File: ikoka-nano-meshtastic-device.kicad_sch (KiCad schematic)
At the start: 10 parts, among them J1 JST_2mm_LiPo, J2 JST_2mm_LiPo, J3 Qwiic_RA, U1 Seeed Studio XIAO nRF52840, U2 E22-900M30S

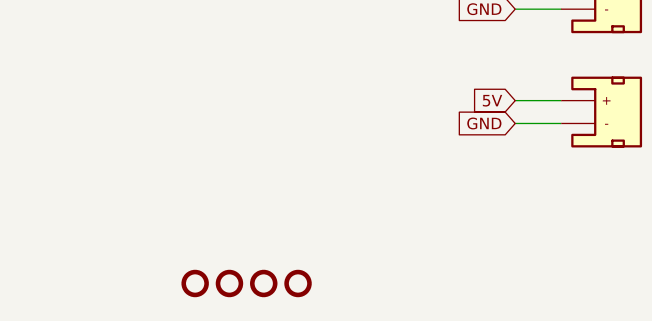
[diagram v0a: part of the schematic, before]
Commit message: Update schematic with LCSC part numbers
Signed-off-by: Andrew Yong <me@ndoo.sg>
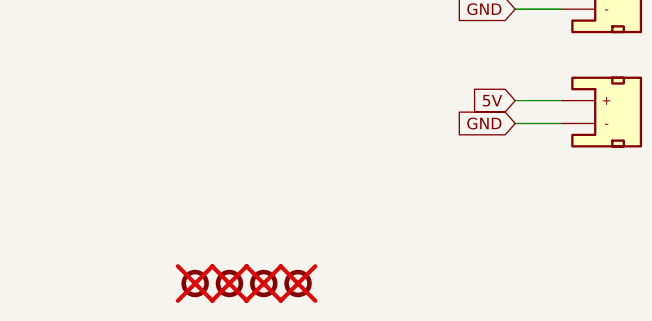
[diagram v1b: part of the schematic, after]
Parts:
- C1: LCSC (none) -> C77085
- J1, J2: LCSC (none) -> C295747
- J3: LCSC (none) -> C160404
- ST1, ST2, ST3, ST4: now not fitted; now left out of the parts list
- U1: LCSC (none) -> C17209540
- U2: LCSC (none) -> C411294
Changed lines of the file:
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@@
   )
   (symbol (lib_id "SparkFun-Hardware:Standoff") (at 55.88 151.13 0) (unit 1)
-    (in_bom yes) (on_board yes) (dnp no) (fields_autoplaced)
+    (in_bom no) (on_board yes) (dnp yes) (fields_autoplaced)
     (property "Reference" "ST1" (at 55.88 148.59 0)
       (effects (font (size 1.27 1.27)) hide)
@@
   )
   (symbol (lib_id "SparkFun-Hardware:Standoff") (at 67.31 151.13 0) (unit 1)
-    (in_bom yes) (on_board yes) (dnp no) (fields_autoplaced)
+    (in_bom no) (on_board yes) (dnp yes) (fields_autoplaced)
     (property "Reference" "ST4" (at 67.31 148.59 0)
       (effects (font (size 1.27 1.27)) hide)
@@
     )
     (property "PROD_ID" "CONN-13694" (at 180.34 133.35 0)
+      (effects (font (size 1.27 1.27)) hide)
+    )
+    (property "LCSC" "C160404" (at 180.34 123.19 0)
       (effects (font (size 1.27 1.27)) hide)
     )
@@
   )
   (symbol (lib_id "SparkFun-Hardware:Standoff") (at 63.5 151.13 0) (unit 1)
-    (in_bom yes) (on_board yes) (dnp no) (fields_autoplaced)
+    (in_bom no) (on_board yes) (dnp yes) (fields_autoplaced)
     (property "Reference" "ST3" (at 63.5 148.59 0)
       (effects (font (size 1.27 1.27)) hide)
@@
   )
   (symbol (lib_id "SparkFun-Hardware:Standoff") (at 59.69 151.13 0) (unit 1)
-    (in_bom yes) (on_board yes) (dnp no) (fields_autoplaced)
+    (in_bom no) (on_board yes) (dnp yes) (fields_autoplaced)
     (property "Reference" "ST2" (at 59.69 148.59 0)
       (effects (font (size 1.27 1.27)) hide)
@@
     )
     (property "PROD_ID" "CONN-11443" (at 101.6 134.62 0)
+      (effects (font (size 1.27 1.27)) hide)
+    )
+    (property "LCSC" "C295747" (at 101.6 118.11 0)
       (effects (font (size 1.27 1.27)) hide)
     )
@@
     (property "MANUFACTURER" "EBYTE" (at 196.85 63.5 0)
       (effects (font (size 1.27 1.27)) (justify bottom) hide)
+    )
+    (property "LCSC" "C411294" (at 196.85 63.5 0)
+      (effects (font (size 1.27 1.27)) hide)
     )
     (pin "8")
@@
       (effects (font (size 0.508 0.508)) hide)
     )
+    (property "LCSC" "C77085" (at 223.52 43.18 0)
+      (effects (font (size 1.27 1.27)) hide)
+    )
     (pin "2")
     (pin "1")
@@
     )
     (property "PROD_ID" "CONN-11443" (at 101.6 147.32 0)
+      (effects (font (size 1.27 1.27)) hide)
+    )
+    (property "LCSC" "C295747" (at 101.6 130.81 0)
       (effects (font (size 1.27 1.27)) hide)
     )
@@
       (effects (font (size 1.27 1.27)) hide)
     )
+    (property "LCSC" "C17209540" (at 81.28 59.69 0)
+      (effects (font (size 1.27 1.27)) hide)
+    )

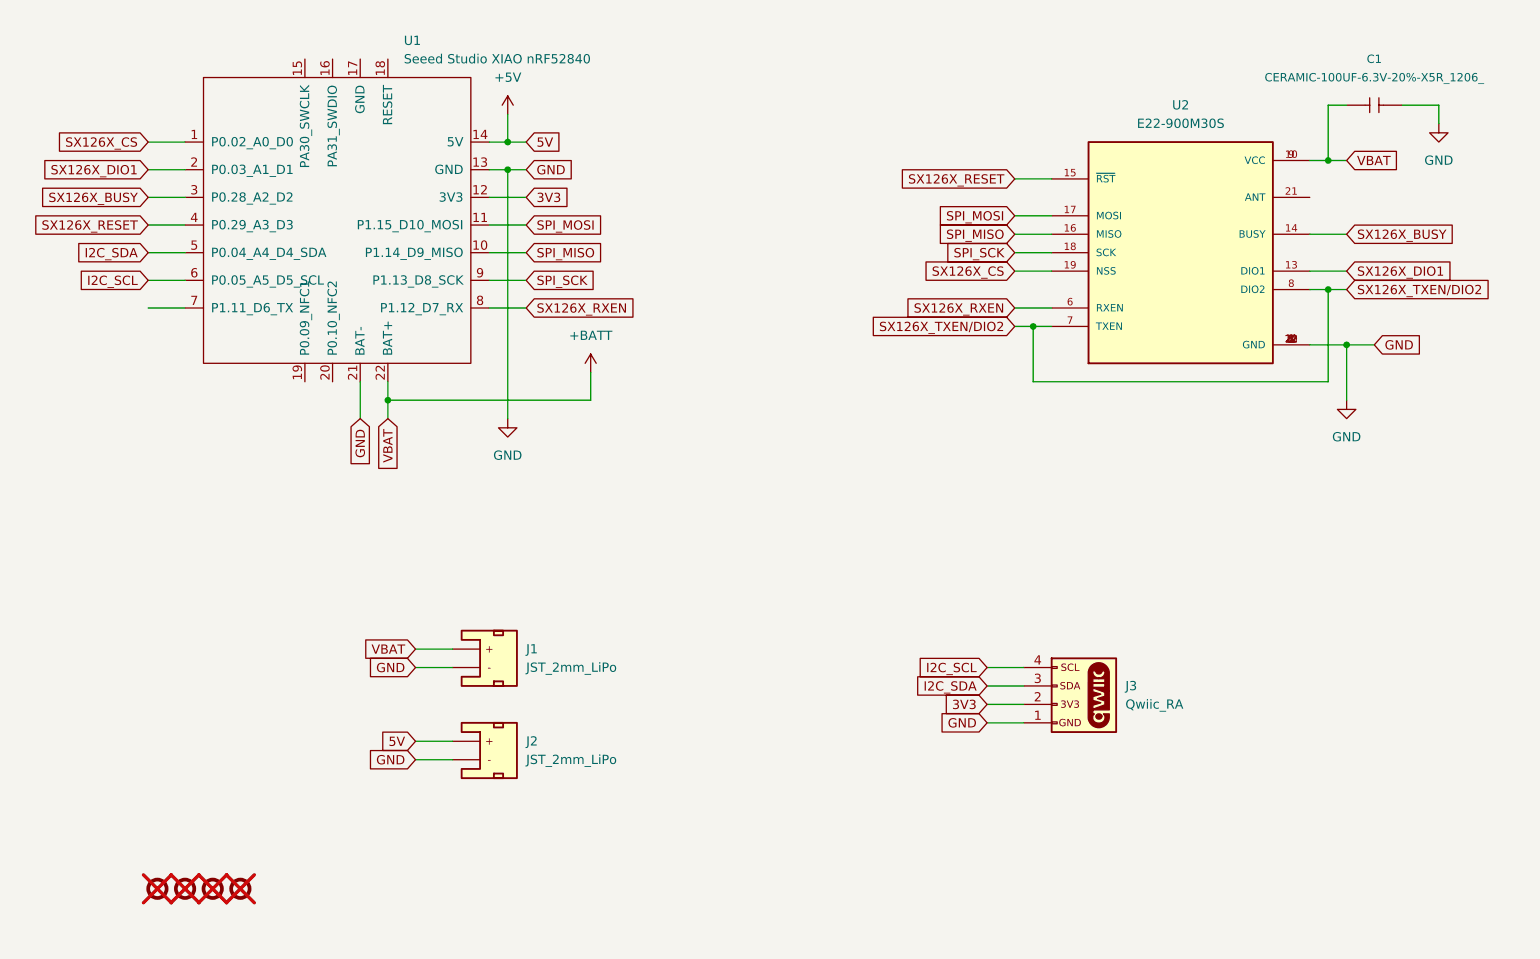
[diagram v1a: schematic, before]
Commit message: Power EBYTE E22 module from 5V and remove JST-PH 2.0 connectors
Power EBYTE E22 module from 5V because VBAT results in very poor transmit power.

Remove JST connectors since the device no longer functions without 5V.

Signed-off-by: Andrew Yong <me@ndoo.sg>
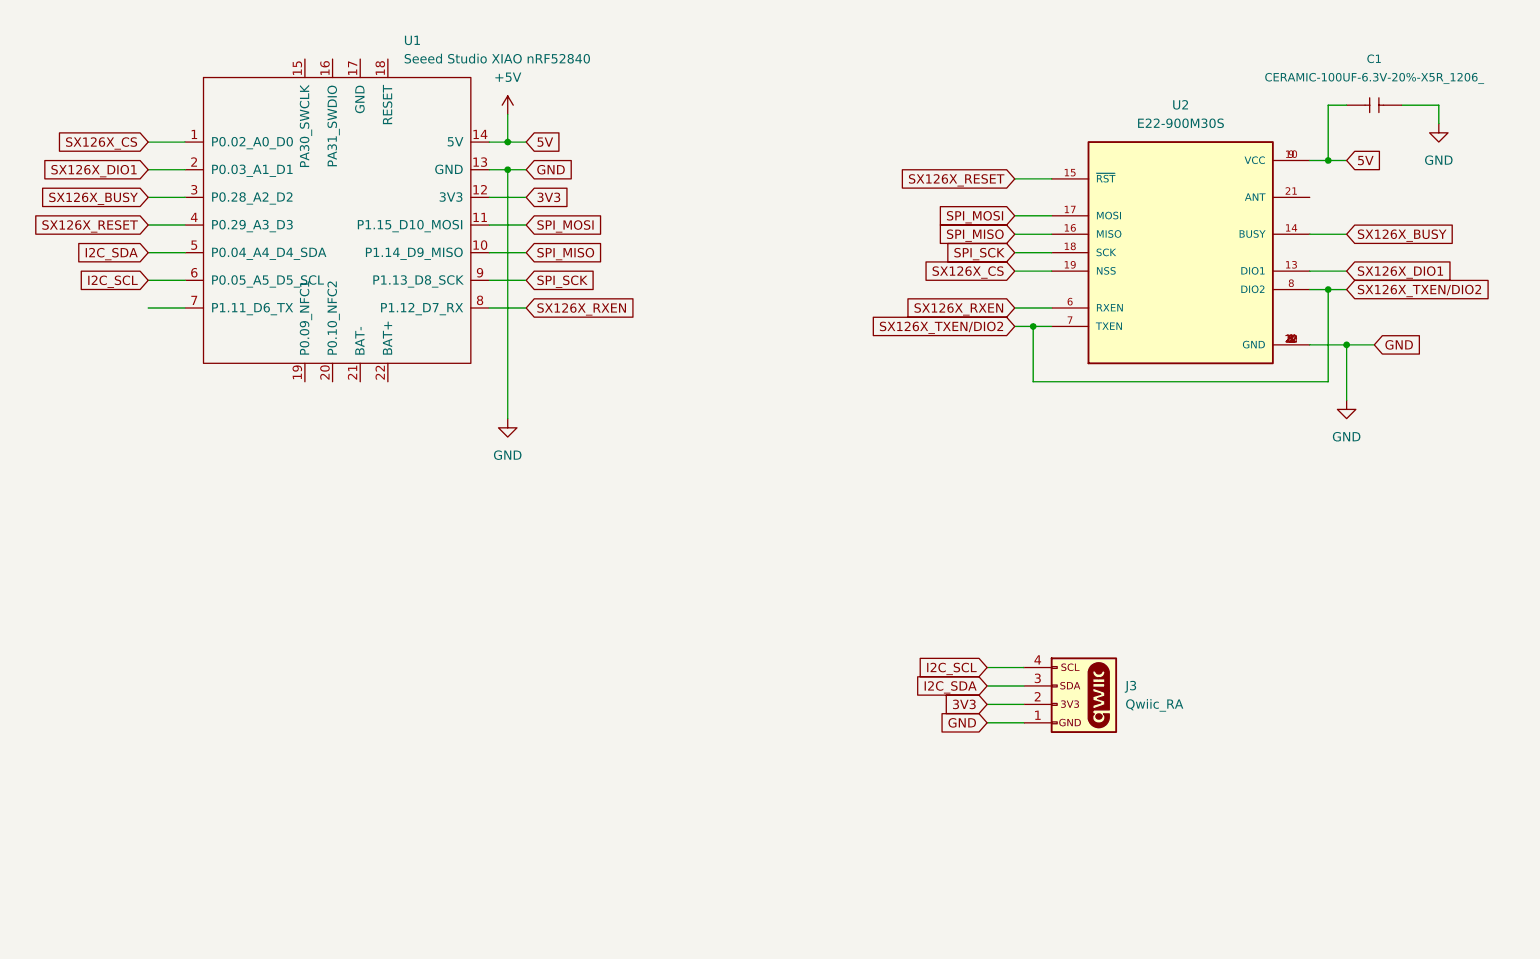
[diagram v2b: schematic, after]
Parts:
- removed J1, J2: JST_2mm_LiPo, SparkFun-Connector:JST_SMD_2.0mm-2, symbol SparkFun-Connector:Conn_01x02_JST_2mm_LiPo
- removed ST1, ST2, ST3, ST4: Standoff, SparkFun-Hardware:Standoff, symbol SparkFun-Hardware:Standoff
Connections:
- net +5V: now also C1.2, U2.10 (VCC), U2.9 (VCC)
- net GND: no longer U1.21 (BAT-)
- removed net +BATT: C1.2, U1.22 (BAT+), U2.10 (VCC), U2.9 (VCC)

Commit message: Add Molex Picoblade 1.25x2 connectors for VBAT and VBUS, add load switch for E22 module power
Signed-off-by: Andrew Yong <me@ndoo.sg>
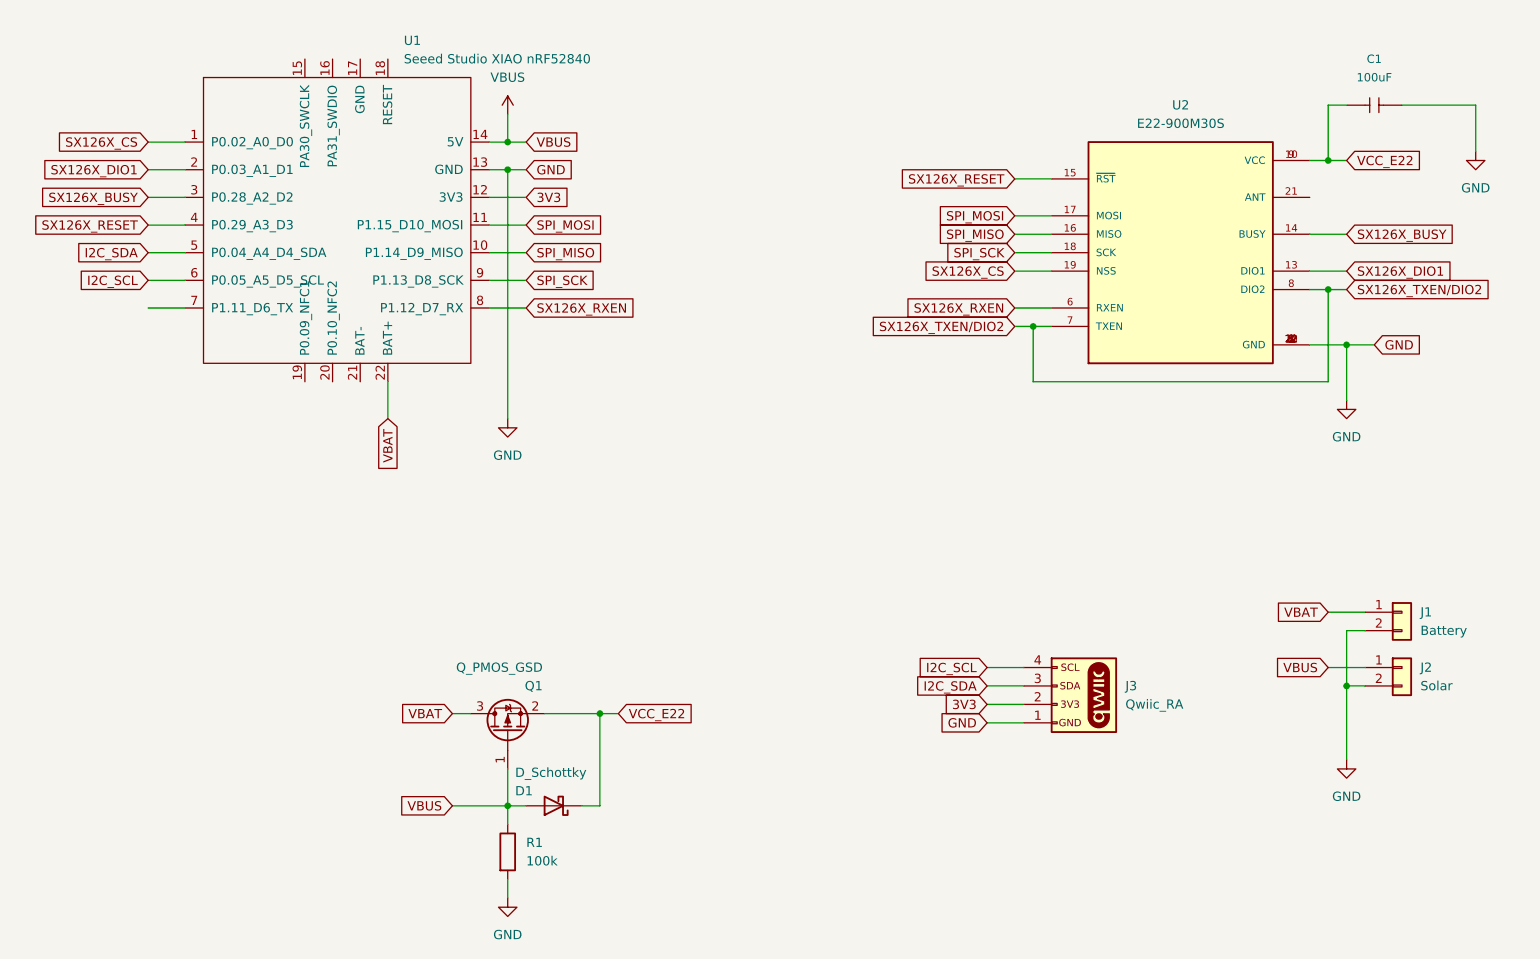
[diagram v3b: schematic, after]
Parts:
- added D1: D_Schottky, symbol Device:D_Schottky
- added J1: Battery, Connector_Molex:Molex_PicoBlade_53261-0271_1x02-1MP_P1.25mm_Horizontal, symbol Connector_Generic:Conn_01x02
- added J2: Solar, Connector_Molex:Molex_PicoBlade_53261-0271_1x02-1MP_P1.25mm_Horizontal, symbol Connector_Generic:Conn_01x02
- added Q1: Q_PMOS_GSD, Package_TO_SOT_SMD:SOT-23-3, symbol Device:Q_PMOS_GSD
- added R1: 100k, symbol Device:R
- C1: value CERAMIC-100UF-6.3V-20%-X5R_1206_ -> 100uF; footprint OPL_Capacitor:C1206 -> Capacitor_SMD:C_1206_3216Metric_Pad1.33x1.80mm_HandSolder
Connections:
- net GND: now also J1.2 (Pin_2), J2.2 (Pin_2), R1.2
- net VBAT: now reaches U1.22 (BAT+)
- net VBAT: now also J1.1 (Pin_1), Q1.3 (D)
- net +5V renamed VCC_E22
- net VCC_E22: now also D1.1 (K), Q1.2 (S); no longer U1.14 (5V)
- new net VBUS: D1.2 (A), J2.1 (Pin_1), Q1.1 (G), R1.1, U1.14 (5V)
